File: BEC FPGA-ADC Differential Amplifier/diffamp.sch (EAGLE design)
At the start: 16 parts, among them U1 ADA4807-2ARMZRM_8-M

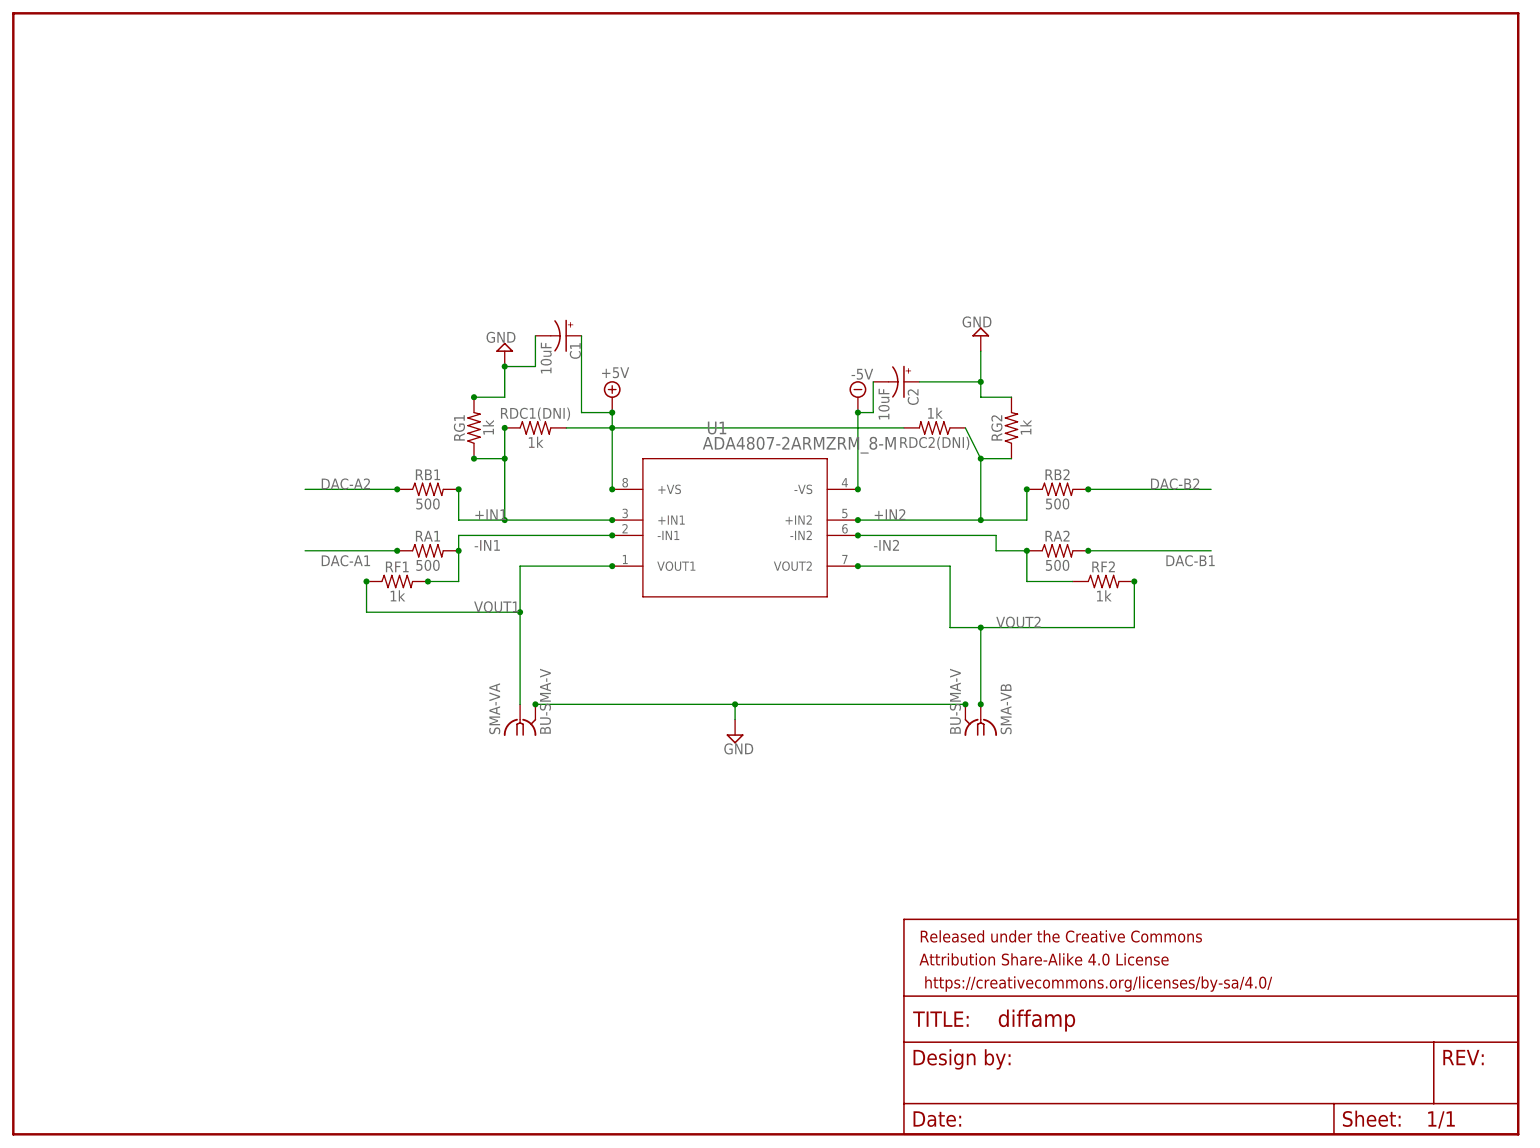
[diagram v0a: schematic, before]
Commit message: Updated differential amplifier circuit. About to begin rewiring. Also removing extra connectors, single port access and that's all.
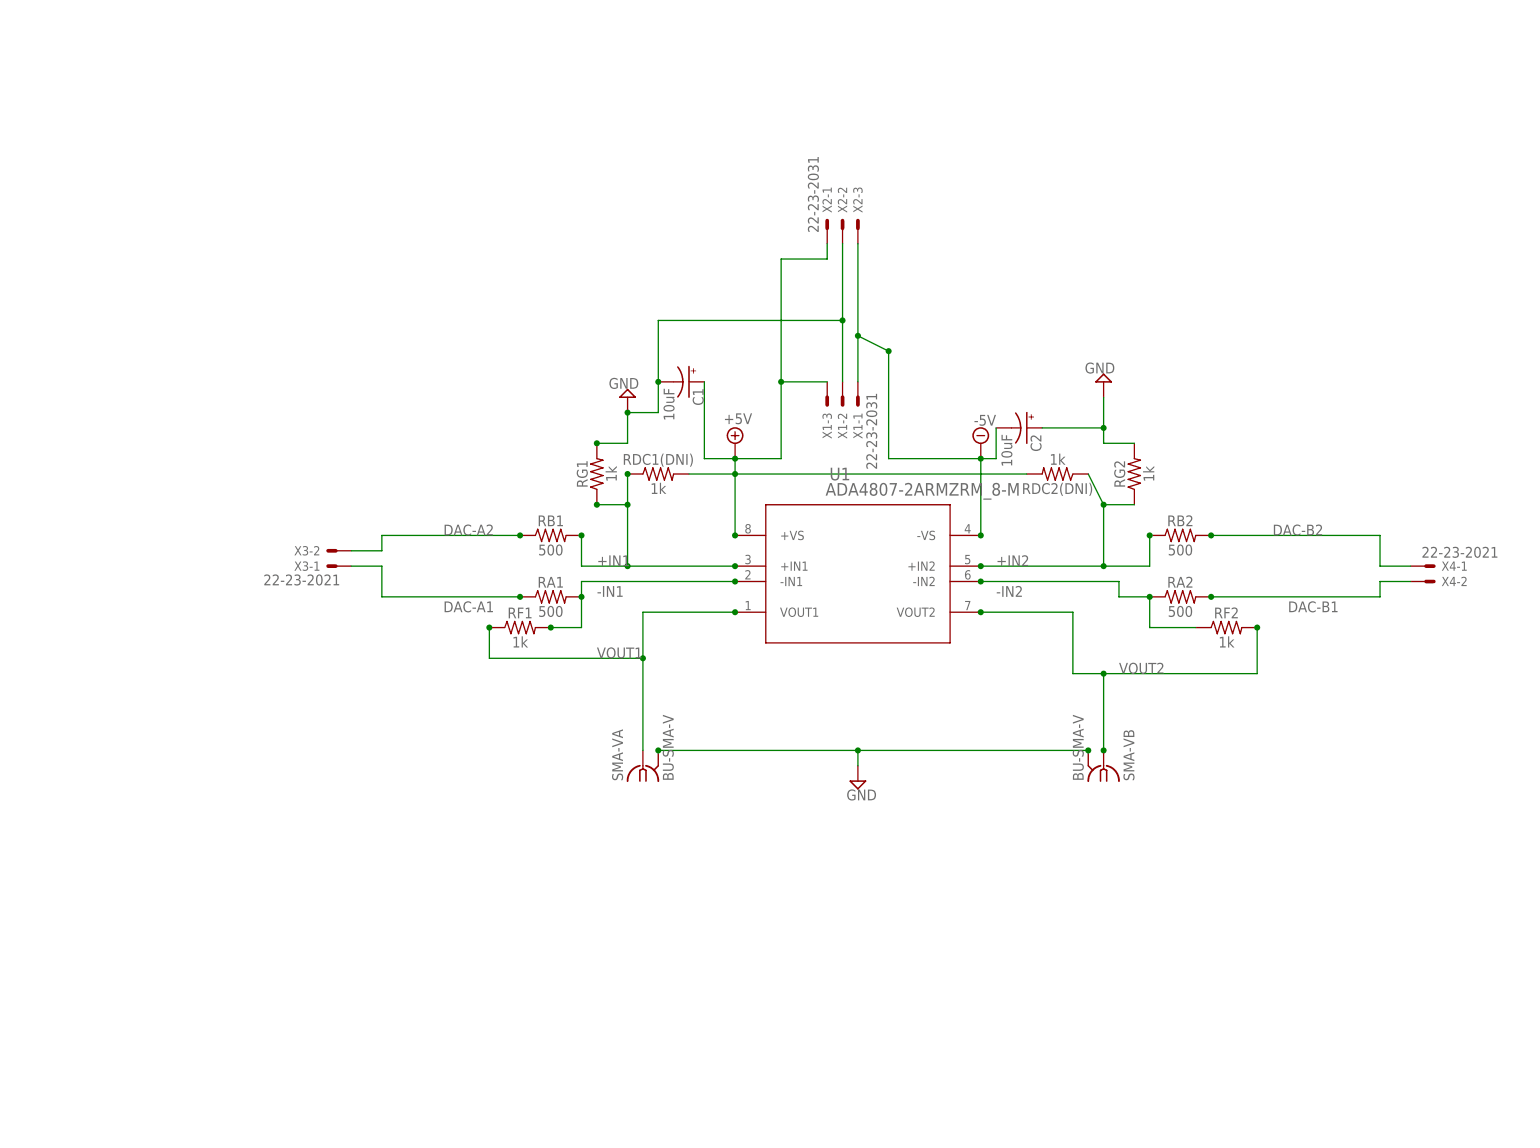
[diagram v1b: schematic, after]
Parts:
- removed FRAME1: FRAME-LETTER, SparkFun-Aesthetics:FRAME-LETTER
- added X1, X2: 22-23-2031, con-molex:22-23-2031
- added X3, X4: 22-23-2021, con-molex:22-23-2021
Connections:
- net +5V: now also X1-3.S, X2-1.S
- net -5V: now also X1-1.S, X2-3.S
- net DAC-A1: now also X3-1.S
- net DAC-A2: now also X3-2.S
- net DAC-B1: now also X4-2.S
- net DAC-B2: now also X4-1.S
- net GND: now also X1-2.S, X2-2.S
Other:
- moved on the sheet: C1, C2, RA1, RA2, RB1, RB2, RDC1(DNI), RDC2(DNI), RF1, RF2, RG1, RG2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

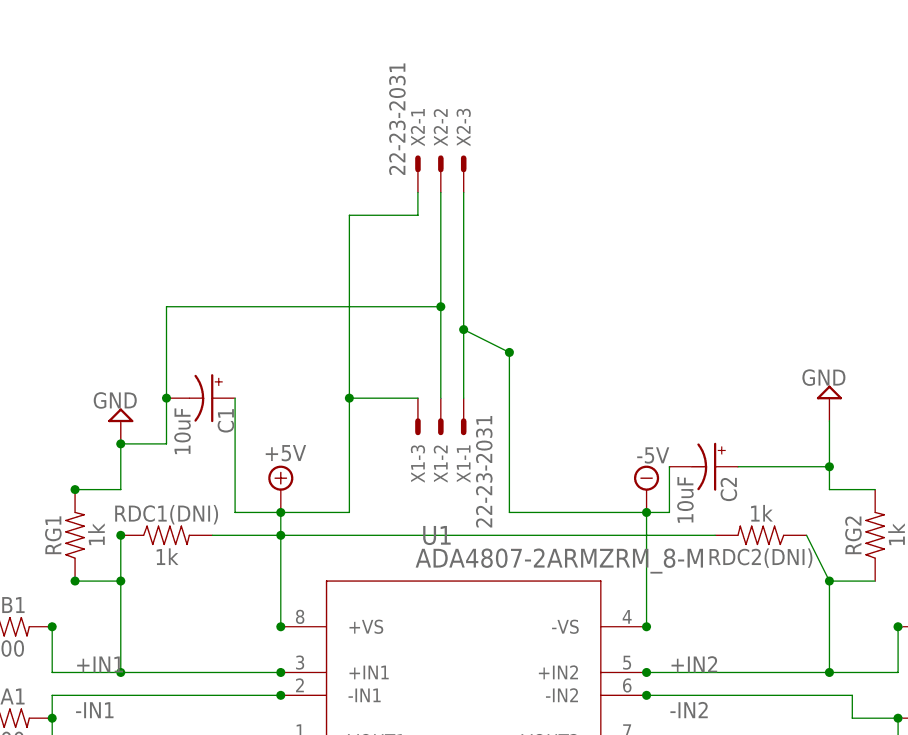
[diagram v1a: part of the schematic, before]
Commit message: Added new source capacitors.
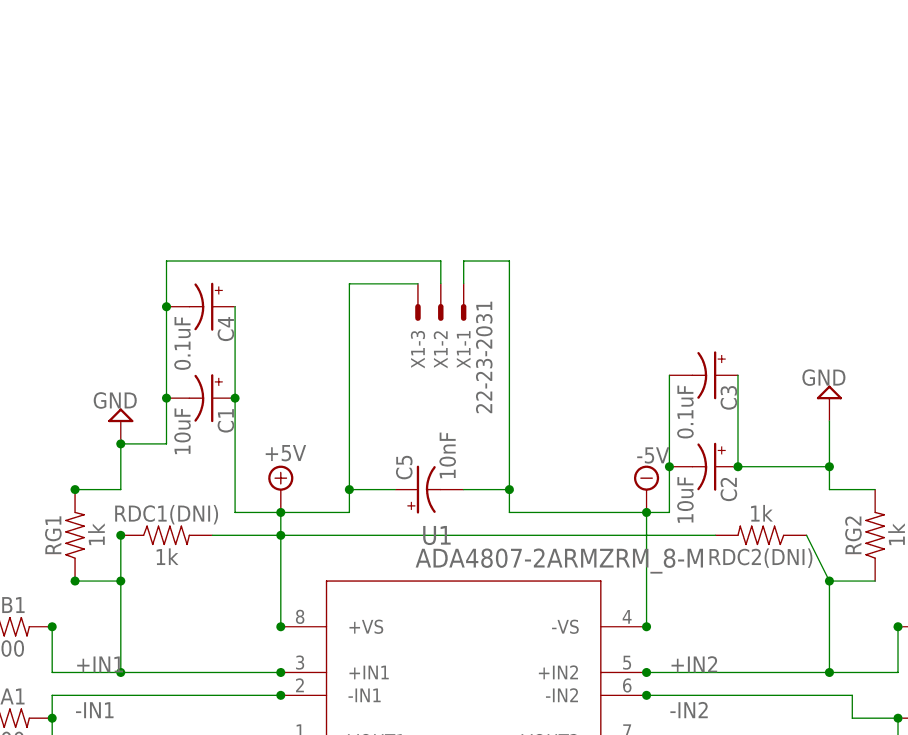
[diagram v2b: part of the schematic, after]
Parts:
- removed X2: 22-23-2031, con-molex:22-23-2031
- added C3, C4: 0.1uF, SparkFun-Capacitors:10UF-POLAR-RADIAL-2.5MM-25V-20%
- added C5: 10nF, SparkFun-Capacitors:10UF-POLAR-RADIAL-2.5MM-25V-20%
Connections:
- net +5V: now also C4.+, C5.+; no longer X2-1.S
- net -5V: now also C3.-, C5.-; no longer X2-3.S
- net GND: now also C3.+, C4.-; no longer X2-2.S
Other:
- moved on the sheet: X1-1, X1-2, X1-3
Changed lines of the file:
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@@
 <part name="C2" library="SparkFun-Capacitors" deviceset="10UF-POLAR" device="-RADIAL-2.5MM-25V-20%" value="10uF"/>
 <part name="X1" library="con-molex" library_urn="urn:adsk.eagle:library:165" deviceset="22-23-2031" device=""/>
-<part name="X2" library="con-molex" library_urn="urn:adsk.eagle:library:165" deviceset="22-23-2031" device=""/>
 <part name="X3" library="con-molex" library_urn="urn:adsk.eagle:library:165" deviceset="22-23-2021" device=""/>
 <part name="X4" library="con-molex" library_urn="urn:adsk.eagle:library:165" deviceset="22-23-2021" device=""/>
+<part name="C5" library="SparkFun-Capacitors" deviceset="10UF-POLAR" device="-RADIAL-2.5MM-25V-20%" value="10nF"/>
+<part name="C3" library="SparkFun-Capacitors" deviceset="10UF-POLAR" device="-RADIAL-2.5MM-25V-20%" value="0.1uF"/>
+<part name="C4" library="SparkFun-Capacitors" deviceset="10UF-POLAR" device="-RADIAL-2.5MM-25V-20%" value="0.1uF"/>
 </parts>
 <sheets>
@@
 <instance part="C1" gate="G$1" x="63.5" y="76.2" rot="R270"/>
 <instance part="C2" gate="G$1" x="119.38" y="68.58" rot="R270"/>
-<instance part="X1" gate="-1" x="91.44" y="73.66" rot="R270"/>
-<instance part="X1" gate="-2" x="88.9" y="73.66" rot="R270"/>
-<instance part="X1" gate="-3" x="86.36" y="73.66" rot="R270"/>
-<instance part="X2" gate="-1" x="86.36" y="101.6" rot="R90"/>
-<instance part="X2" gate="-2" x="88.9" y="101.6" rot="R90"/>
-<instance part="X2" gate="-3" x="91.44" y="101.6" rot="R90"/>
+<instance part="X1" gate="-1" x="91.44" y="86.36" rot="R270"/>
+<instance part="X1" gate="-2" x="88.9" y="86.36" rot="R270"/>
+<instance part="X1" gate="-3" x="86.36" y="86.36" rot="R270"/>
 <instance part="X3" gate="-1" x="5.08" y="45.72" rot="R180"/>
 <instance part="X3" gate="-2" x="5.08" y="48.26" rot="R180"/>
 <instance part="X4" gate="-1" x="185.42" y="45.72"/>
 <instance part="X4" gate="-2" x="185.42" y="43.18"/>
+<instance part="C5" gate="G$1" x="86.36" y="66.04" rot="R90"/>
+<instance part="C3" gate="G$1" x="119.38" y="78.74" rot="R270"/>
+<instance part="C4" gate="G$1" x="63.5" y="86.36" rot="R270"/>
 </instances>
 <busses>
@@
 <pinref part="RDC2(DNI)" gate="G$1" pin="2"/>
 <wire x1="119.38" y1="60.96" x2="71.12" y2="60.96" width="0.1524" layer="91"/>
-<wire x1="78.74" y1="76.2" x2="78.74" y2="63.5" width="0.1524" layer="91"/>
+<wire x1="78.74" y1="88.9" x2="78.74" y2="66.04" width="0.1524" layer="91"/>
+<wire x1="78.74" y1="66.04" x2="78.74" y2="63.5" width="0.1524" layer="91"/>
 <wire x1="78.74" y1="63.5" x2="71.12" y2="63.5" width="0.1524" layer="91"/>
-<wire x1="78.74" y1="96.52" x2="78.74" y2="76.2" width="0.1524" layer="91"/>
 <pinref part="RDC1(DNI)" gate="G$1" pin="2"/>
 <wire x1="63.5" y1="60.96" x2="71.12" y2="60.96" width="0.1524" layer="91"/>
 <pinref part="X1" gate="-3" pin="S"/>
-<wire x1="78.74" y1="76.2" x2="86.36" y2="76.2" width="0.1524" layer="91"/>
-<junction x="78.74" y="76.2"/>
-<wire x1="78.74" y1="96.52" x2="86.36" y2="96.52" width="0.1524" layer="91"/>
-<pinref part="X2" gate="-1" pin="S"/>
-<wire x1="86.36" y1="96.52" x2="86.36" y2="99.06" width="0.1524" layer="91"/>
+<wire x1="78.74" y1="88.9" x2="86.36" y2="88.9" width="0.1524" layer="91"/>
+<pinref part="C5" gate="G$1" pin="+"/>
+<wire x1="83.82" y1="66.04" x2="78.74" y2="66.04" width="0.1524" layer="91"/>
+<junction x="78.74" y="66.04"/>
+<pinref part="C4" gate="G$1" pin="+"/>
+<wire x1="66.04" y1="86.36" x2="66.04" y2="76.2" width="0.1524" layer="91"/>
+<junction x="66.04" y="76.2"/>
 </segment>
 </net>
@@
 <wire x1="114.3" y1="63.5" x2="114.3" y2="68.58" width="0.1524" layer="91"/>
 <junction x="111.76" y="63.5"/>
-<wire x1="96.52" y1="81.28" x2="96.52" y2="63.5" width="0.1524" layer="91"/>
+<wire x1="96.52" y1="91.44" x2="96.52" y2="66.04" width="0.1524" layer="91"/>
+<wire x1="96.52" y1="66.04" x2="96.52" y2="63.5" width="0.1524" layer="91"/>
 <wire x1="96.52" y1="63.5" x2="111.76" y2="63.5" width="0.1524" layer="91"/>
-<wire x1="91.44" y1="99.06" x2="91.44" y2="83.82" width="0.1524" layer="91"/>
-<junction x="96.52" y="81.28"/>
 <pinref part="X1" gate="-1" pin="S"/>
-<wire x1="96.52" y1="81.28" x2="91.44" y2="83.82" width="0.1524" layer="91"/>
-<wire x1="91.44" y1="83.82" x2="91.44" y2="76.2" width="0.1524" layer="91"/>
-<pinref part="X2" gate="-3" pin="S"/>
-<junction x="91.44" y="83.82"/>
+<wire x1="96.52" y1="91.44" x2="91.44" y2="91.44" width="0.1524" layer="91"/>
+<wire x1="91.44" y1="91.44" x2="91.44" y2="88.9" width="0.1524" layer="91"/>
+<pinref part="C5" gate="G$1" pin="-"/>
+<wire x1="91.44" y1="66.04" x2="96.52" y2="66.04" width="0.1524" layer="91"/>
+<junction x="96.52" y="66.04"/>
+<pinref part="C3" gate="G$1" pin="-"/>
+<wire x1="114.3" y1="78.74" x2="114.3" y2="68.58" width="0.1524" layer="91"/>
+<junction x="114.3" y="68.58"/>
 </segment>
 </net>
@@
 <wire x1="121.92" y1="68.58" x2="132.08" y2="68.58" width="0.1524" layer="91"/>
 <junction x="132.08" y="68.58"/>
+<pinref part="C3" gate="G$1" pin="+"/>
+<wire x1="121.92" y1="78.74" x2="121.92" y2="68.58" width="0.1524" layer="91"/>
+<junction x="121.92" y="68.58"/>
 </segment>
 <segment>
@@
 <wire x1="58.42" y1="76.2" x2="58.42" y2="71.12" width="0.1524" layer="91"/>
 <wire x1="58.42" y1="71.12" x2="53.34" y2="71.12" width="0.1524" layer="91"/>
-<wire x1="88.9" y1="86.36" x2="88.9" y2="76.2" width="0.1524" layer="91"/>
-<wire x1="88.9" y1="86.36" x2="58.42" y2="86.36" width="0.1524" layer="91"/>
-<wire x1="58.42" y1="86.36" x2="58.42" y2="76.2" width="0.1524" layer="91"/>
+<wire x1="88.9" y1="91.44" x2="88.9" y2="88.9" width="0.1524" layer="91"/>
+<wire x1="88.9" y1="91.44" x2="58.42" y2="91.44" width="0.1524" layer="91"/>
+<wire x1="58.42" y1="91.44" x2="58.42" y2="86.36" width="0.1524" layer="91"/>
 <junction x="58.42" y="76.2"/>
 <pinref part="X1" gate="-2" pin="S"/>
-<pinref part="X2" gate="-2" pin="S"/>
-<wire x1="88.9" y1="86.36" x2="88.9" y2="99.06" width="0.1524" layer="91"/>
-<junction x="88.9" y="86.36"/>
+<pinref part="C4" gate="G$1" pin="-"/>
+<wire x1="58.42" y1="86.36" x2="58.42" y2="76.2" width="0.1524" layer="91"/>
+<junction x="58.42" y="86.36"/>
 </segment>
 </net>

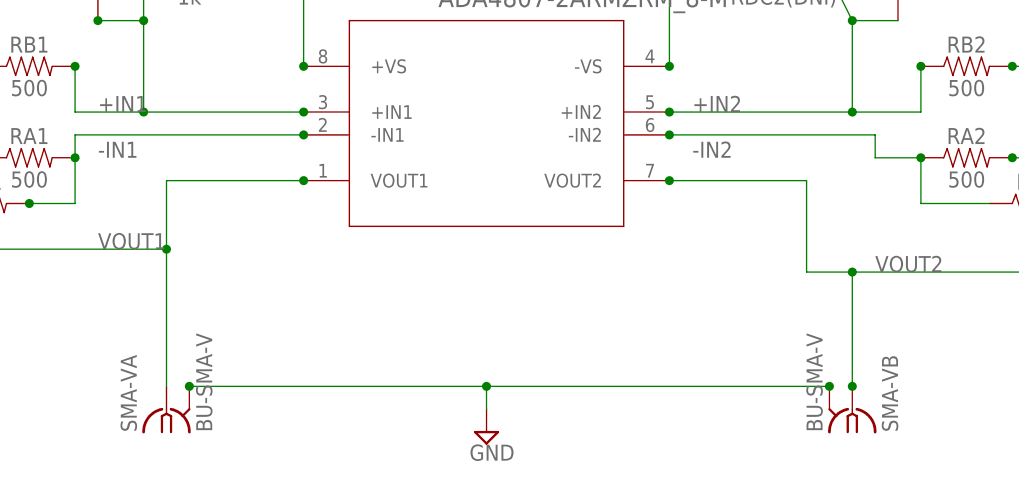
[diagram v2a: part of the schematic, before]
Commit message: Added output series resistance. Not Routed
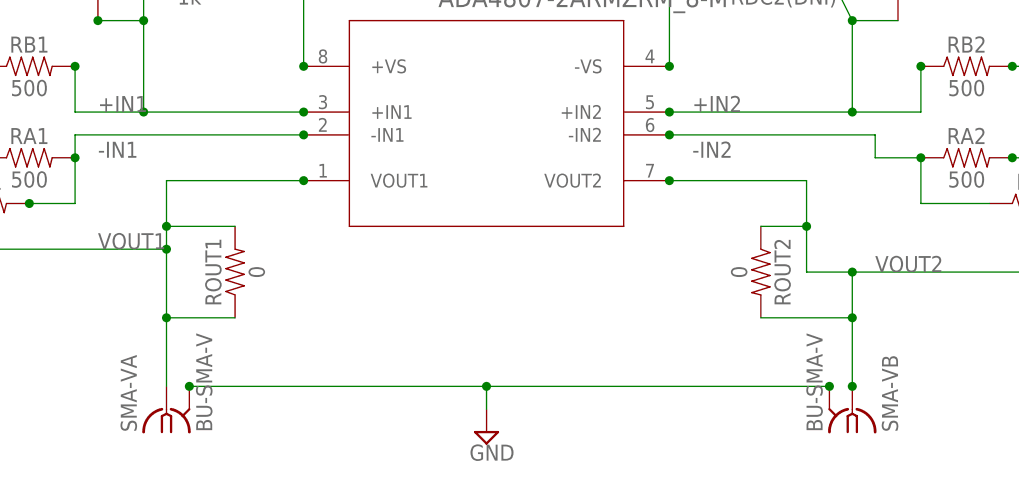
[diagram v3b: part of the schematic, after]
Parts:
- added ROUT1, ROUT2: 0, SparkFun-Resistors:RESISTORAXIAL-0.3
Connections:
- net VOUT1: now also ROUT1.1, ROUT1.2
- net VOUT2: now also ROUT2.1, ROUT2.2
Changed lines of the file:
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@@
 <part name="C3" library="SparkFun-Capacitors" deviceset="10UF-POLAR" device="-RADIAL-2.5MM-25V-20%" value="0.1uF"/>
 <part name="C4" library="SparkFun-Capacitors" deviceset="10UF-POLAR" device="-RADIAL-2.5MM-25V-20%" value="0.1uF"/>
+<part name="ROUT1" library="SparkFun-Resistors" deviceset="RESISTOR" device="AXIAL-0.3" value="0"/>
+<part name="ROUT2" library="SparkFun-Resistors" deviceset="RESISTOR" device="AXIAL-0.3" value="0"/>
 </parts>
 <sheets>
@@
 <instance part="C3" gate="G$1" x="119.38" y="78.74" rot="R270"/>
 <instance part="C4" gate="G$1" x="63.5" y="86.36" rot="R270"/>
+<instance part="ROUT1" gate="G$1" x="63.5" y="27.94" rot="R90"/>
+<instance part="ROUT2" gate="G$1" x="121.92" y="27.94" rot="R270"/>
 </instances>
 <busses>
@@
 <pinref part="RF1" gate="G$1" pin="1"/>
 <pinref part="U1" gate="A" pin="VOUT1"/>
-<wire x1="55.88" y1="30.48" x2="55.88" y2="38.1" width="0.1524" layer="91"/>
+<wire x1="55.88" y1="30.48" x2="55.88" y2="33.02" width="0.1524" layer="91"/>
+<wire x1="55.88" y1="33.02" x2="55.88" y2="38.1" width="0.1524" layer="91"/>
 <wire x1="55.88" y1="38.1" x2="71.12" y2="38.1" width="0.1524" layer="91"/>
 <pinref part="SMA-VA" gate="G$1" pin="1"/>
 <wire x1="30.48" y1="30.48" x2="55.88" y2="30.48" width="0.1524" layer="91"/>
-<wire x1="55.88" y1="15.24" x2="55.88" y2="30.48" width="0.1524" layer="91"/>
+<wire x1="55.88" y1="15.24" x2="55.88" y2="22.86" width="0.1524" layer="91"/>
+<wire x1="55.88" y1="22.86" x2="55.88" y2="30.48" width="0.1524" layer="91"/>
 <wire x1="30.48" y1="35.56" x2="30.48" y2="30.48" width="0.1524" layer="91"/>
 <junction x="55.88" y="30.48"/>
@@
 <junction x="30.48" y="35.56"/>
 <junction x="71.12" y="38.1"/>
+<pinref part="ROUT1" gate="G$1" pin="1"/>
+<wire x1="55.88" y1="22.86" x2="63.5" y2="22.86" width="0.1524" layer="91"/>
+<junction x="55.88" y="22.86"/>
+<pinref part="ROUT1" gate="G$1" pin="2"/>
+<wire x1="63.5" y1="33.02" x2="55.88" y2="33.02" width="0.1524" layer="91"/>
+<junction x="55.88" y="33.02"/>
 </segment>
 </net>
@@
 <pinref part="U1" gate="A" pin="VOUT2"/>
 <wire x1="111.76" y1="38.1" x2="127" y2="38.1" width="0.1524" layer="91"/>
-<wire x1="127" y1="38.1" x2="127" y2="27.94" width="0.1524" layer="91"/>
+<wire x1="127" y1="38.1" x2="127" y2="33.02" width="0.1524" layer="91"/>
+<wire x1="127" y1="33.02" x2="127" y2="27.94" width="0.1524" layer="91"/>
 <wire x1="127" y1="27.94" x2="132.08" y2="27.94" width="0.1524" layer="91"/>
 <wire x1="132.08" y1="27.94" x2="157.48" y2="27.94" width="0.1524" layer="91"/>
@@
 <pinref part="RF2" gate="G$1" pin="2"/>
 <pinref part="SMA-VB" gate="G$1" pin="1"/>
-<wire x1="132.08" y1="15.24" x2="132.08" y2="27.94" width="0.1524" layer="91"/>
+<wire x1="132.08" y1="15.24" x2="132.08" y2="22.86" width="0.1524" layer="91"/>
 <junction x="132.08" y="27.94"/>
 <label x="134.62" y="27.94" size="1.778" layer="95"/>
@@
 <junction x="157.48" y="35.56"/>
 <junction x="132.08" y="15.24"/>
-</segment>
-</net>
+<pinref part="ROUT2" gate="G$1" pin="1"/>
+<wire x1="132.08" y1="22.86" x2="132.08" y2="27.94" width="0.1524" layer="91"/>
+<wire x1="121.92" y1="33.02" x2="127" y2="33.02" width="0.1524" layer="91"/>
+<junction x="127" y="33.02"/>
+<pinref part="ROUT2" gate="G$1" pin="2"/>
+<wire x1="121.92" y1="22.86" x2="132.08" y2="22.86" width="0.1524" layer="91"/>
+<junction x="132.08" y="22.86"/>
+</segment>
+</net>
